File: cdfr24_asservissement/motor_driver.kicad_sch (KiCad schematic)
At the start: 21 parts

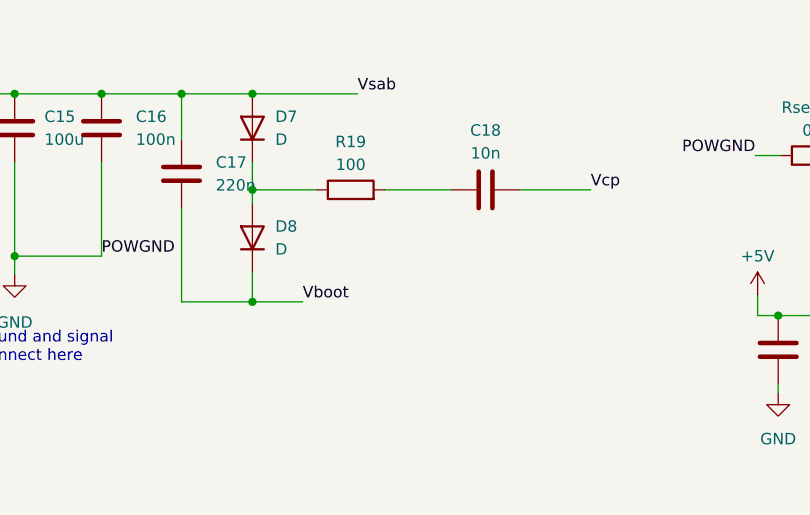
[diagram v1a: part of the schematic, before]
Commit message: Add footprints
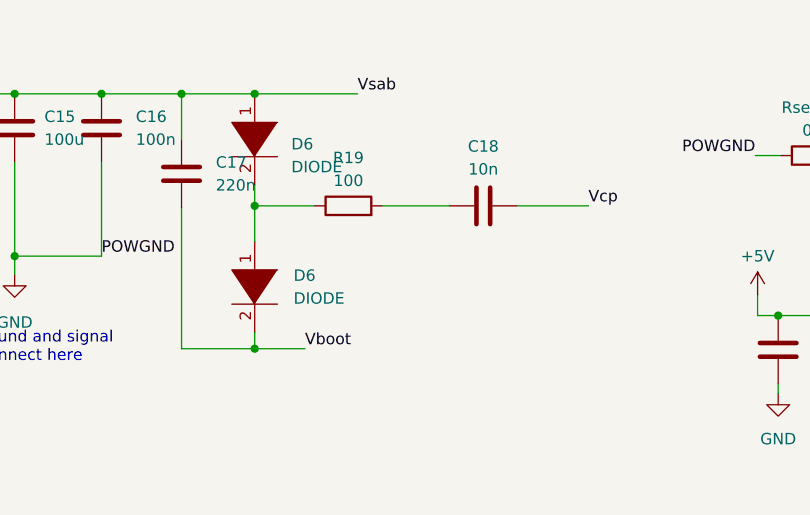
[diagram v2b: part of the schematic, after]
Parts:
- removed D7, D8: D, symbol Device:D
- added D6 (x2): DIODE, B170B:DIOM505270X240, symbol pspice:DIODE
- C15: footprint (none) -> Capacitor_SMD:CP_Elec_10x10.5
- C16, C17, C18, C19, Cen1, Coff1, Cpul1: footprint (none) -> Capacitor_SMD:C_0805_2012Metric_Pad1.18x1.45mm_HandSolder
- CR1: footprint SO-24_STM -> L6235D:SO-24_STM
- R19, R20, RH1, RH2, RH3, Ren1, Ren2, Roff1, Rpul1, Rsense1: footprint (none) -> Resistor_SMD:R_0805_2012Metric_Pad1.20x1.40mm_HandSolder
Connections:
- net +BATT: now also D6.1 (K)
- net Vboot: now also D6.2 (A)
- net at R19.1: now also D6.1 (K), D6.2 (A)
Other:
- moved on the sheet: C18, R19

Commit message: Place PCB components
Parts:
- Rsense1: footprint Resistor_SMD:R_0805_2012Metric_Pad1.20x1.40mm_HandSolder -> Resistor_SMD:R_2512_6332Metric
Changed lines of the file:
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@@
       (effects (font (size 1.27 1.27)))
     )
-    (property "Footprint" "Resistor_SMD:R_0805_2012Metric_Pad1.20x1.40mm_HandSolder" (at 231.648 35.052 90)
+    (property "Footprint" "Resistor_SMD:R_2512_6332Metric" (at 231.648 35.052 90)
       (effects (font (size 1.27 1.27)) hide)
     )
